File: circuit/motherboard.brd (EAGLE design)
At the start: 67 x 64.8 mm, 19 parts, among them IC1 ATMEGA8

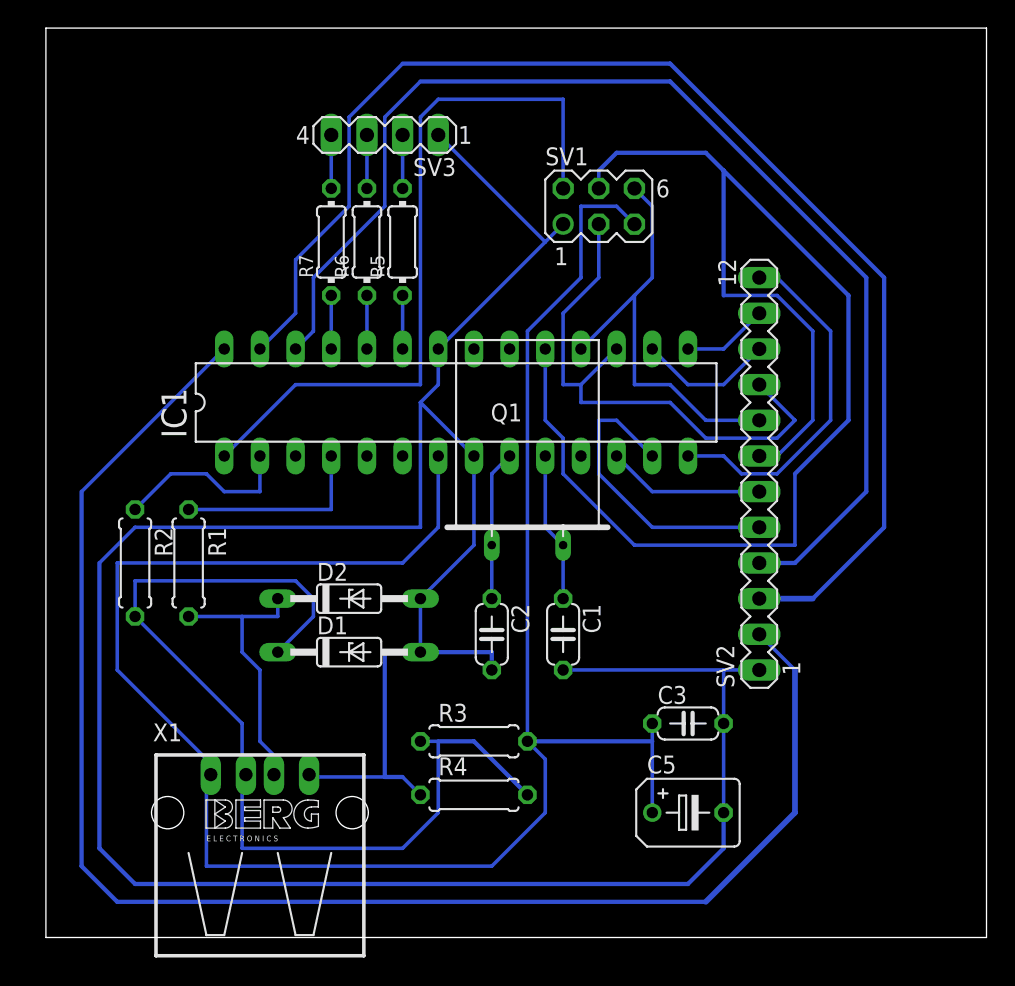
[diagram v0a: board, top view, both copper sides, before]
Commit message: New PCB design, minor chenges in schematic
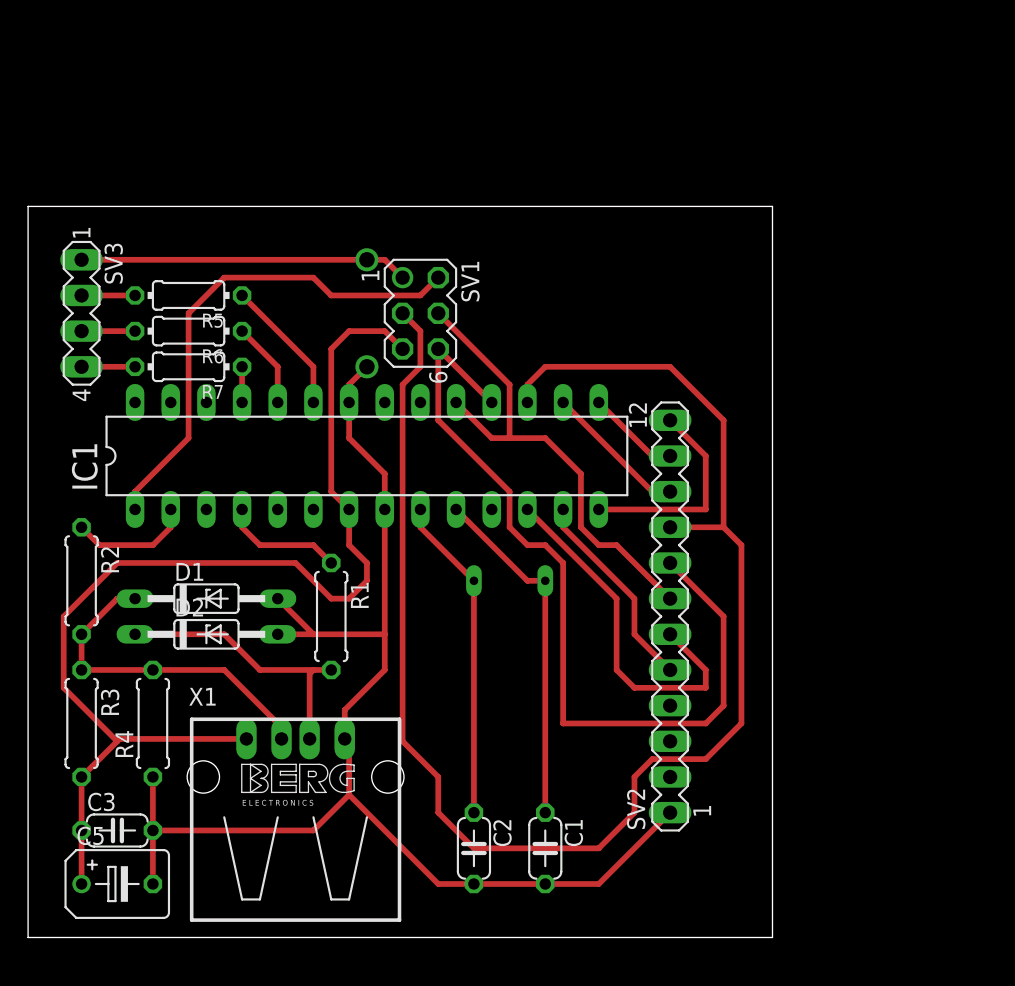
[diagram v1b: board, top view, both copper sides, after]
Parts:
- moved C3 41.3 mm to (5.08, 7.62)
- moved C5 41.0 mm to (5.08, 3.81)
- moved R3 28.0 mm to (2.54, 15.2), turned to 270 degrees
- moved SV3 25.0 mm to (2.54, 44.5), turned to 270 degrees
- moved R4 23.4 mm to (7.62, 15.2), turned to 90 degrees
- moved Q1 17.8 mm to (33.0, 17.8), flipped to the bottom, turned to 180 degrees
- moved R5 15.7 mm to (10.2, 45.7), turned to 180 degrees
- moved C1 15.3 mm to (35.6, 6.35)
- moved C2 15.3 mm to (30.5, 6.35)
- moved SV1 14.8 mm to (26.7, 44.5), turned to 270 degrees
- moved R6 14.2 mm to (10.2, 43.2), turned to 180 degrees
- moved R7 13.5 mm to (10.2, 40.6), turned to 180 degrees
- moved SV2 12.0 mm to (44.5, 22.9)
- moved R1 10.9 mm to (20.3, 22.9)
- moved D1 10.9 mm to (11.4, 24.1)
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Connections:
- new net N$25: SV2.2
- new net N$26: SV2.3
- new net N$27: SV2.4
- net N$15: no longer SV2.4
- net N$16: no longer SV2.3
- net N$17: no longer SV2.2
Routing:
- net N$17: track 109.3 -> 0.00 mm
- net N$16: track 93.9 -> 0.00 mm
- net N$15: track 85.2 -> 0.00 mm
- net GND: track 201.2 -> 118.2 mm
- net N$10: track 39.0 -> 108.7 mm
- net VCC: track 144.0 -> 79.4 mm
- net N$7: track 98.7 -> 34.3 mm
- net N$1: track 69.8 -> 24.1 mm
- net N$23: track 30.4 -> 60.2 mm
- net N$18: track 52.2 -> 35.4 mm
- net N$13: track 11.2 -> 25.8 mm
- net N$5: track 10.7 -> 25.0 mm
- net N$6: track 10.7 -> 23.2 mm
- net N$8: track 25.3 -> 15.0 mm
- net N$14: track 21.7 -> 14.6 mm
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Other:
- board size 67 x 64.8 mm -> 53 x 52.1 mm

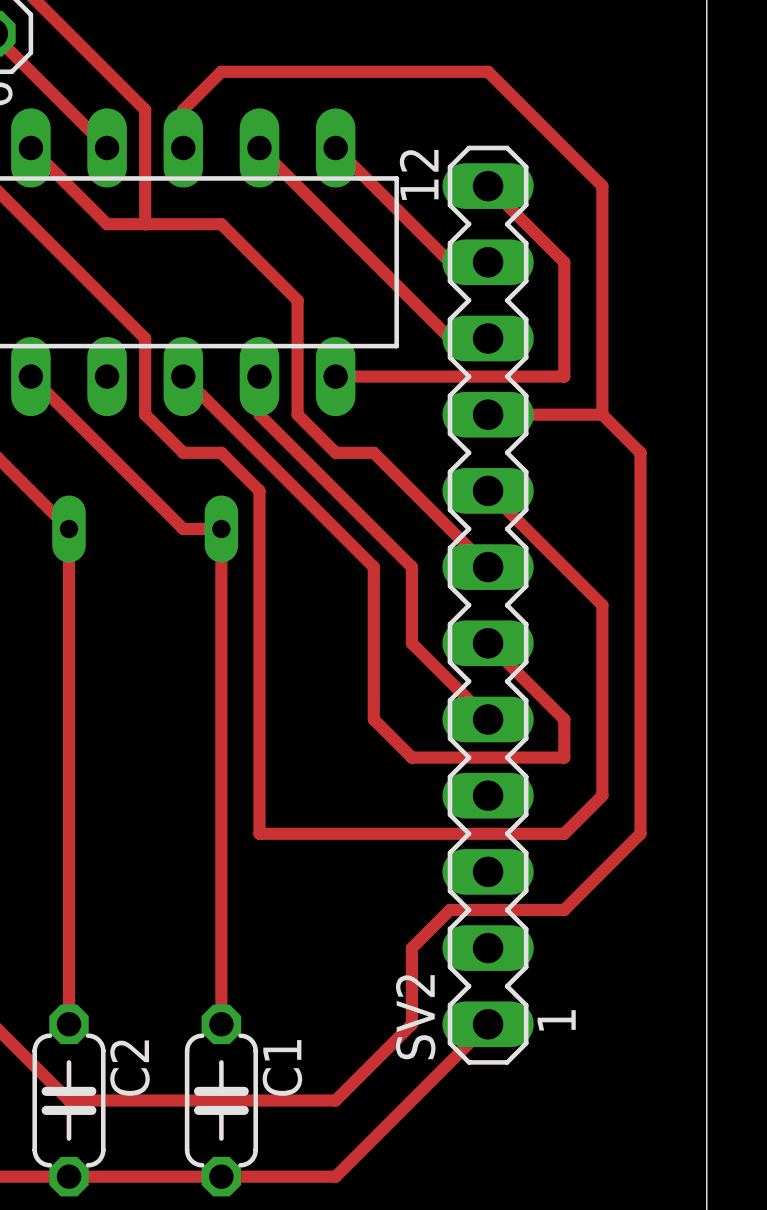
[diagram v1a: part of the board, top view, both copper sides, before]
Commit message: a couple of design rule checks fixed (not all)
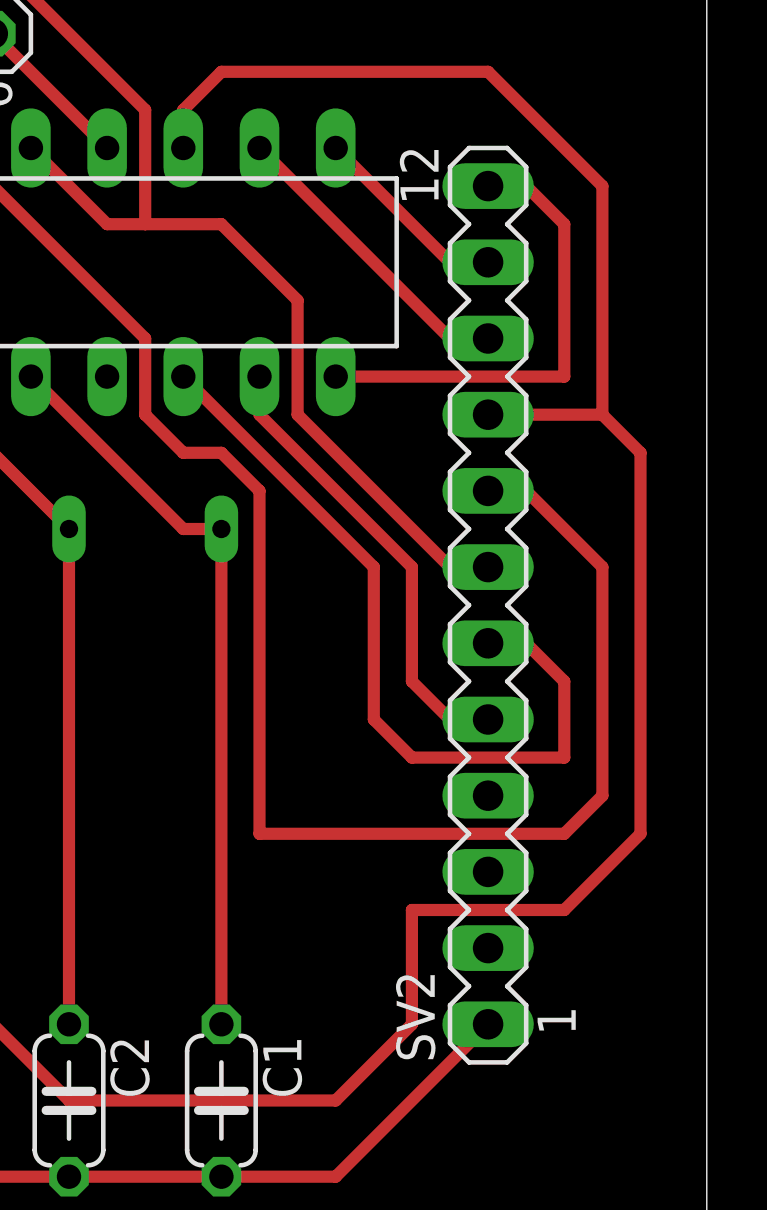
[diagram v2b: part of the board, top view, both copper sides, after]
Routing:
- net N$10: track 108.7 -> 109.5 mm
- net N$14: track 14.6 -> 15.3 mm
- net N$8: track 15.0 -> 15.8 mm
- net N$13: track 25.8 -> 26.5 mm
- net N$23: track 60.2 -> 60.9 mm
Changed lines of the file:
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@@
 <layer number="17" name="Pads" color="2" fill="1" visible="yes" active="yes"/>
 <layer number="18" name="Vias" color="2" fill="1" visible="yes" active="yes"/>
-<layer number="19" name="Unrouted" color="6" fill="1" visible="no" active="yes"/>
+<layer number="19" name="Unrouted" color="6" fill="1" visible="yes" active="yes"/>
 <layer number="20" name="Dimension" color="15" fill="1" visible="yes" active="yes"/>
 <layer number="21" name="tPlace" color="7" fill="1" visible="no" active="yes"/>
@@
 </class>
 </classes>
-<designrules name="default">
+<designrules name="default *">
 <description language="de">&lt;b&gt;EAGLE Design Rules&lt;/b&gt;
 &lt;p&gt;
@@
 <param name="mtCopper" value="0.035mm 0.035mm 0.035mm 0.035mm 0.035mm 0.035mm 0.035mm 0.035mm 0.035mm 0.035mm 0.035mm 0.035mm 0.035mm 0.035mm 0.035mm 0.035mm"/>
 <param name="mtIsolate" value="1.5mm 0.15mm 0.2mm 0.15mm 0.2mm 0.15mm 0.2mm 0.15mm 0.2mm 0.15mm 0.2mm 0.15mm 0.2mm 0.15mm 0.2mm"/>
-<param name="mdWireWire" value="8mil"/>
-<param name="mdWirePad" value="8mil"/>
-<param name="mdWireVia" value="8mil"/>
-<param name="mdPadPad" value="8mil"/>
-<param name="mdPadVia" value="8mil"/>
-<param name="mdViaVia" value="8mil"/>
-<param name="mdSmdPad" value="8mil"/>
-<param name="mdSmdVia" value="8mil"/>
-<param name="mdSmdSmd" value="8mil"/>
+<param name="mdWireWire" value="16mil"/>
+<param name="mdWirePad" value="16mil"/>
+<param name="mdWireVia" value="16mil"/>
+<param name="mdPadPad" value="16mil"/>
+<param name="mdPadVia" value="16mil"/>
+<param name="mdViaVia" value="16mil"/>
+<param name="mdSmdPad" value="16mil"/>
+<param name="mdSmdVia" value="16mil"/>
+<param name="mdSmdSmd" value="16mil"/>
 <param name="mdViaViaSameLayer" value="8mil"/>
 <param name="mnLayersViaInSmd" value="2"/>
@@
 <contactref element="SV2" pad="12"/>
 <wire x1="46.99" y1="30.48" x2="39.37" y2="30.48" width="0.4064" layer="1"/>
-<wire x1="46.99" y1="34.29" x2="46.99" y2="30.48" width="0.4064" layer="1"/>
-<wire x1="44.45" y1="36.83" x2="46.99" y2="34.29" width="0.4064" layer="1"/>
+<wire x1="46.99" y1="35.56" x2="46.99" y2="30.48" width="0.4064" layer="1"/>
+<wire x1="46.99" y1="35.56" x2="45.72" y2="36.83" width="0.4064" layer="1"/>
+<wire x1="45.72" y1="36.83" x2="44.45" y2="36.83" width="0.4064" layer="1"/>
 </signal>
 <signal name="N$7">
@@
 <wire x1="33.02" y1="39.37" x2="33.02" y2="35.56" width="0.4064" layer="1"/>
 <wire x1="27.94" y1="44.45" x2="33.02" y2="39.37" width="0.4064" layer="1"/>
-<wire x1="40.64" y1="27.94" x2="44.45" y2="24.13" width="0.4064" layer="1"/>
-<wire x1="39.37" y1="27.94" x2="40.64" y2="27.94" width="0.4064" layer="1"/>
-<wire x1="38.1" y1="29.21" x2="39.37" y2="27.94" width="0.4064" layer="1"/>
 <wire x1="38.1" y1="33.02" x2="38.1" y2="29.21" width="0.4064" layer="1"/>
 <wire x1="38.1" y1="33.02" x2="35.56" y2="35.56" width="0.4064" layer="1"/>
 <wire x1="35.56" y1="35.56" x2="33.02" y2="35.56" width="0.4064" layer="1"/>
+<wire x1="38.1" y1="29.21" x2="43.18" y2="24.13" width="0.4064" layer="1"/>
+<wire x1="43.18" y1="24.13" x2="44.45" y2="24.13" width="0.4064" layer="1"/>
 </signal>
 <signal name="N$10">
@@
 <wire x1="25.4" y1="39.37" x2="26.67" y2="40.64" width="0.4064" layer="1"/>
 <wire x1="25.4" y1="13.97" x2="25.4" y2="39.37" width="0.4064" layer="1"/>
-<wire x1="43.18" y1="12.7" x2="41.91" y2="11.43" width="0.4064" layer="1"/>
-<wire x1="46.99" y1="12.7" x2="43.18" y2="12.7" width="0.4064" layer="1"/>
+<wire x1="46.99" y1="12.7" x2="41.91" y2="12.7" width="0.4064" layer="1"/>
 <wire x1="49.53" y1="27.94" x2="49.53" y2="15.24" width="0.4064" layer="1"/>
 <wire x1="48.26" y1="29.21" x2="49.53" y2="27.94" width="0.4064" layer="1"/>
 <wire x1="30.48" y1="6.35" x2="39.37" y2="6.35" width="0.4064" layer="1"/>
 <wire x1="39.37" y1="6.35" x2="41.91" y2="8.89" width="0.4064" layer="1"/>
-<wire x1="41.91" y1="8.89" x2="41.91" y2="11.43" width="0.4064" layer="1"/>
+<wire x1="41.91" y1="8.89" x2="41.91" y2="12.7" width="0.4064" layer="1"/>
 <wire x1="46.99" y1="12.7" x2="49.53" y2="15.24" width="0.4064" layer="1"/>
 <wire x1="30.48" y1="6.35" x2="27.94" y2="8.89" width="0.4064" layer="1"/>
@@
 <wire x1="40.64" y1="19.05" x2="40.64" y2="24.13" width="0.4064" layer="1"/>
 <wire x1="46.99" y1="17.78" x2="41.91" y2="17.78" width="0.4064" layer="1"/>
-<wire x1="46.99" y1="19.05" x2="46.99" y2="17.78" width="0.4064" layer="1"/>
-<wire x1="44.45" y1="21.59" x2="46.99" y2="19.05" width="0.4064" layer="1"/>
 <wire x1="41.91" y1="17.78" x2="40.64" y2="19.05" width="0.4064" layer="1"/>
+<wire x1="46.99" y1="17.78" x2="46.99" y2="20.32" width="0.4064" layer="1"/>
+<wire x1="46.99" y1="20.32" x2="45.72" y2="21.59" width="0.4064" layer="1"/>
+<wire x1="45.72" y1="21.59" x2="44.45" y2="21.59" width="0.4064" layer="1"/>
 </signal>
 <signal name="N$14">
@@
 <wire x1="36.83" y1="29.21" x2="36.83" y2="30.48" width="0.4064" layer="1"/>
 <wire x1="41.91" y1="24.13" x2="36.83" y2="29.21" width="0.4064" layer="1"/>
-<wire x1="41.91" y1="21.59" x2="41.91" y2="24.13" width="0.4064" layer="1"/>
-<wire x1="44.45" y1="19.05" x2="41.91" y2="21.59" width="0.4064" layer="1"/>
+<wire x1="41.91" y1="20.32" x2="41.91" y2="24.13" width="0.4064" layer="1"/>
+<wire x1="41.91" y1="20.32" x2="43.18" y2="19.05" width="0.4064" layer="1"/>
+<wire x1="43.18" y1="19.05" x2="44.45" y2="19.05" width="0.4064" layer="1"/>
 </signal>
 <signal name="N$15">
@@
 <contactref element="SV2" pad="8"/>
 <wire x1="27.94" y1="41.91" x2="31.75" y2="38.1" width="0.4064" layer="1"/>
-<wire x1="48.26" y1="22.86" x2="44.45" y2="26.67" width="0.4064" layer="1"/>
-<wire x1="48.26" y1="16.51" x2="48.26" y2="22.86" width="0.4064" layer="1"/>
+<wire x1="48.26" y1="16.51" x2="48.26" y2="24.13" width="0.4064" layer="1"/>
 <wire x1="36.83" y1="15.24" x2="46.99" y2="15.24" width="0.4064" layer="1"/>
 <wire x1="36.83" y1="26.67" x2="36.83" y2="15.24" width="0.4064" layer="1"/>
@@
 <wire x1="27.94" y1="41.91" x2="27.94" y2="36.83" width="0.4064" layer="1"/>
 <wire x1="46.99" y1="15.24" x2="48.26" y2="16.51" width="0.4064" layer="1"/>
+<wire x1="48.26" y1="24.13" x2="45.72" y2="26.67" width="0.4064" layer="1"/>
+<wire x1="45.72" y1="26.67" x2="44.45" y2="26.67" width="0.4064" layer="1"/>
 </signal>
 <signal name="N$9">
